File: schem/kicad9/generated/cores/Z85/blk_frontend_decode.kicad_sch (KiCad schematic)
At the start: 0 parts

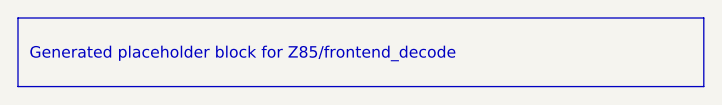
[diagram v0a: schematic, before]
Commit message: kicad: generate core-level hierarchical schematics
Detailed description:
- What changed: regenerated common and core schematics for Z85/Z90/Z380/Z480, Am9513/4/5, Am95xx, and CarbonIO/DMA placeholders
- Why it changed: update generated KiCad 9 outputs to reflect the final naming and tier model
- Files/paths affected: schem/kicad9/generated/common/* and schem/kicad9/generated/cores/*
- How to run it: scripts/gen_kicad.sh (or python tools/kicadgen/src/kicadgen.py)
- What remains TODO: regenerate and commit system-level schematics
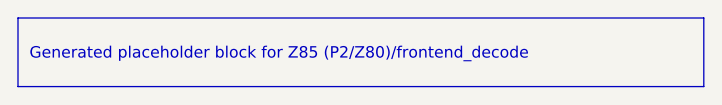
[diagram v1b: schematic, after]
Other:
- title: Z85::frontend_decode -> Z85 (P2/Z80)::frontend_decode
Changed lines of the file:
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@@
 	(version 20250114)
 	(generator "kicadgen")
-	(generator_version "0.1")
+	(generator_version "0.2")
 	(paper "A3")
 	(title_block
-		(title "Z85::frontend_decode")
+		(title "Z85 (P2/Z80)::frontend_decode")
 		(company "Project Carbon")
 		(comment 1 "Generated - do not edit in generated/")
@@
 	)
 	(text_box
-		"Generated placeholder block for Z85/frontend_decode"
+		"Generated placeholder block for Z85 (P2/Z80)/frontend_decode"
 		(exclude_from_sim no)
 		(at
